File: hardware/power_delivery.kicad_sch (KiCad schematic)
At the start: 15 parts, among them J2 24V, U2 LM2596S-ADJ, U3 LM1117-5.0, U4 LM1117-3.3

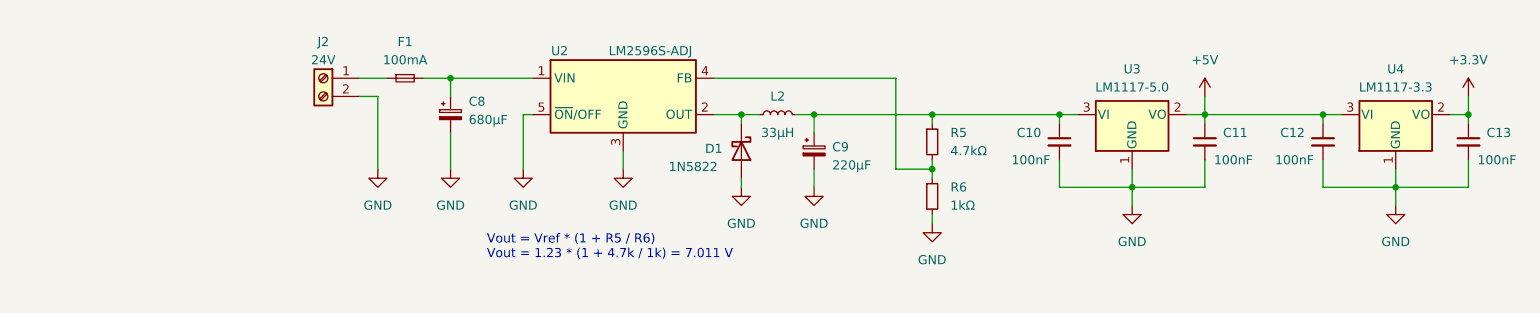
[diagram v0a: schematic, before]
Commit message: Improve the CAN transceiver circuit
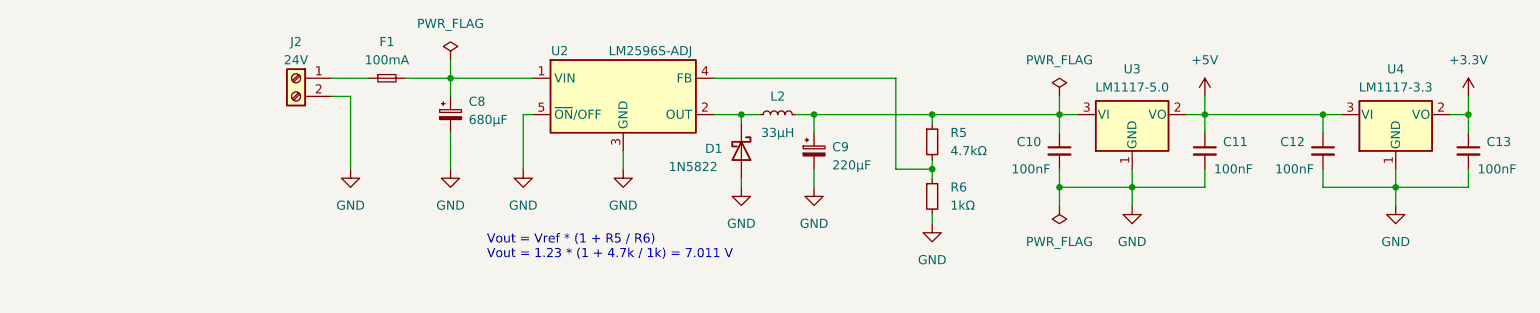
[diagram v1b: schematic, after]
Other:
- company: PUT MotorSport -> PUT Motorsport
- moved on the sheet: C10, C11, C12, C13, F1, J2

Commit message: Add a low-pass filter to the analog circuit supply
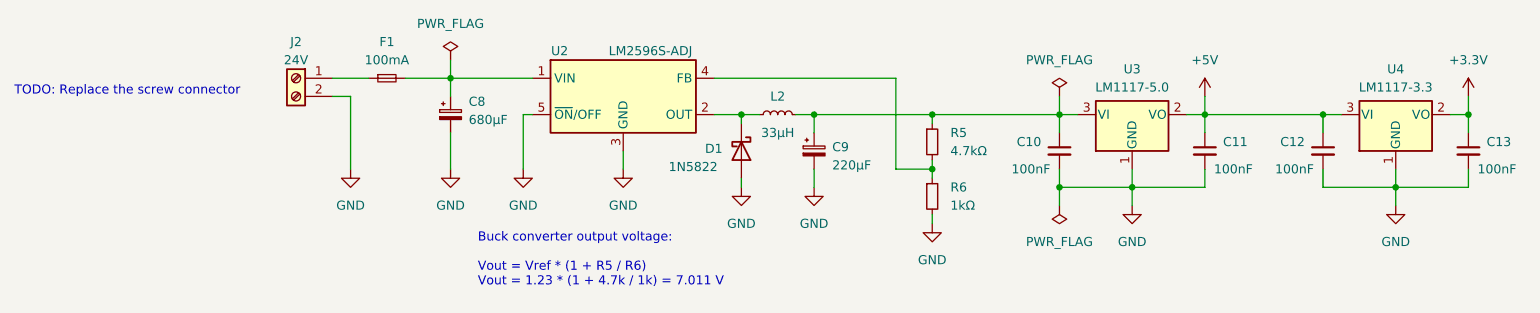
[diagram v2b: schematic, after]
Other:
- note added: "Buck converter output voltage: Vout = Vref * (1 + R5 / R6) Vout = 1.23 * (1 + 4.7k / 1k) = 7.011 V"
- note added: "TODO: Replace the screw connector"
- note removed: "Vout = Vref * (1 + R5 / R6) Vout = 1.23 * (1 + 4.7k / 1k) = 7.011 V"
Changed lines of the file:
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@@
     (stroke (width 0) (type default) (color 0 0 0 0))
   )
-  (text "Vout = Vref * (1 + R5 / R6)\nVout = 1.23 * (1 + 4.7k / 1k) = 7.011 V"
-    (at 90.17 113.03 0)
+  (text "Buck converter output voltage:\n\nVout = Vref * (1 + R5 / R6)\nVout = 1.23 * (1 + 4.7k / 1k) = 7.011 V"
+    (at 88.9 116.84 0)
     (effects (font (size 1.27 1.27)) (justify left bottom))
   )
+  (text "TODO: Replace the screw connector" (at 24.13 90.17 0)
+    (effects (font (size 1.27 1.27)) (justify left bottom))
+  )

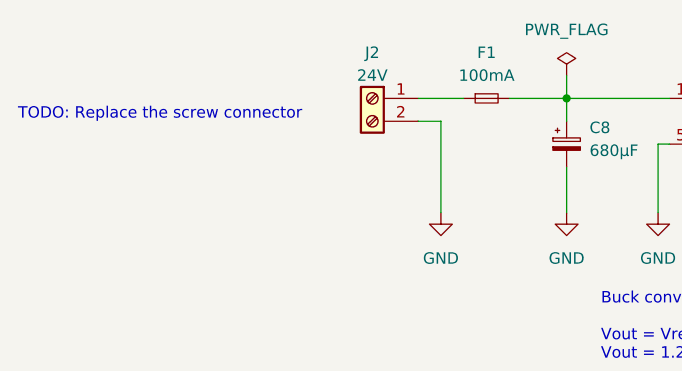
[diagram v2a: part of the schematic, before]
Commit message: Improve power delivery sheet:
- Move power connector to the main sheet
- Use PTC fuse
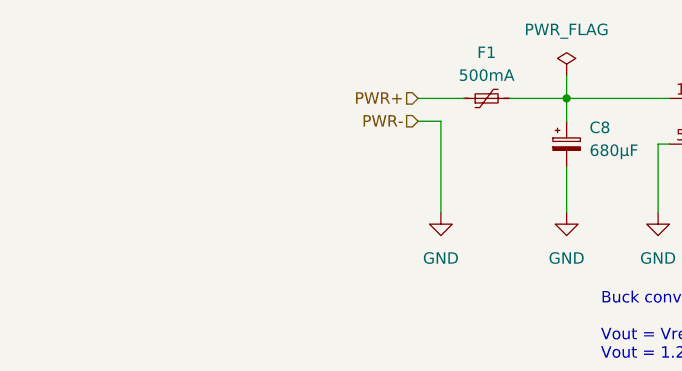
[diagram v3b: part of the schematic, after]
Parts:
- removed F1: 100mA, symbol Device:Fuse_Small
- removed J2: 24V, symbol Connector:Screw_Terminal_01x02
- added F1: 500mA, symbol Device:Polyfuse_Small
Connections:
- net at C8.1, U2.1 (VIN): now also F1.2
- new net PWR+: F1.1
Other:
- note removed: "TODO: Replace the screw connector"
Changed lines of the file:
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@@
     (effects (font (size 1.27 1.27)) (justify left bottom))
   )
-  (text "TODO: Replace the screw connector" (at 24.13 90.17 0)
-    (effects (font (size 1.27 1.27)) (justify left bottom))
+  (hierarchical_label "PWR+" (shape input) (at 68.58 87.63 180)
+    (effects (font (size 1.27 1.27)) (justify right))
+  )
+  (hierarchical_label "PWR-" (shape input) (at 68.58 90.17 180)
+    (effects (font (size 1.27 1.27)) (justify right))
   )
   (symbol (lib_id "power:GND") (at 180.34 105.41 0) (unit 1)
@@
     (pin "1")
   )
-  (symbol (lib_id "Connector:Screw_Terminal_01x02") (at 63.5 87.63 0) (mirror y) (unit 1)
-    (in_bom yes) (on_board yes)
-    (property "Reference" "J2" (id 0) (at 63.5 82.55 0))
-    (property "Value" "24V" (id 1) (at 63.5 85.09 0))
-    (property "Footprint" "" (id 2) (at 63.5 87.63 0)
-      (effects (font (size 1.27 1.27)) hide)
-    )
-    (property "Datasheet" "~" (id 3) (at 63.5 87.63 0)
-      (effects (font (size 1.27 1.27)) hide)
-    )
-    (pin "1")
-    (pin "2")
-  )
   (symbol (lib_id "power:GND") (at 109.22 100.33 0) (unit 1)
     (in_bom yes) (on_board yes) (fields_autoplaced)
@@
     )
     (pin "1")
+  )
+  (symbol (lib_id "Device:Polyfuse_Small") (at 76.2 87.63 90) (unit 1)
+    (in_bom yes) (on_board yes)
+    (property "Reference" "F1" (id 0) (at 76.2 82.55 90))
+    (property "Value" "500mA" (id 1) (at 76.2 85.09 90))
+    (property "Footprint" "" (id 2) (at 81.28 86.36 0)
+      (effects (font (size 1.27 1.27)) (justify left) hide)
+    )
+    (property "Datasheet" "~" (id 3) (at 76.2 87.63 0)
+      (effects (font (size 1.27 1.27)) hide)
+    )
+    (pin "1")
+    (pin "2")
   )
   (symbol (lib_id "Device:C_Small") (at 207.01 97.79 0) (unit 1)
@@
       (effects (font (size 1.27 1.27)) hide)
     )
-    (pin "1")
-    (pin "2")
-  )
-  (symbol (lib_id "Device:Fuse_Small") (at 76.2 87.63 0) (unit 1)
-    (in_bom yes) (on_board yes) (fields_autoplaced)
-    (property "Reference" "F1" (id 0) (at 76.2 82.55 0))
-    (property "Value" "100mA" (id 1) (at 76.2 85.09 0))
-    (property "Footprint" "" (id 2) (at 76.2 87.63 0)
-      (effects (font (size 1.27 1.27)) hide)
-    )
-    (property "Datasheet" "~" (id 3) (at 76.2 87.63 0)
-      (effects (font (size 1.27 1.27)) hide)
-    )

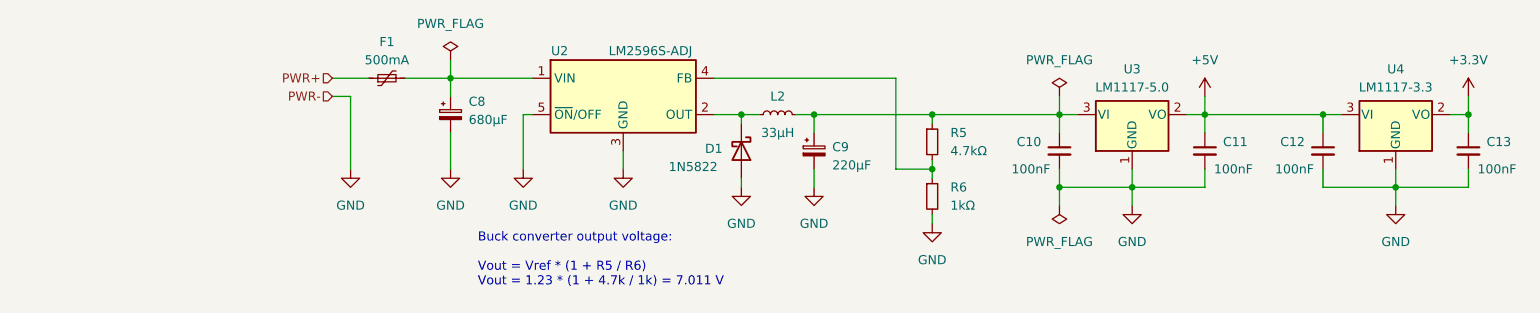
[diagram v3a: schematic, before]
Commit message: Refactor the main sheet
- Replace screw connectors with a goldpin header
- Add reset button
- Add SWD debugger header
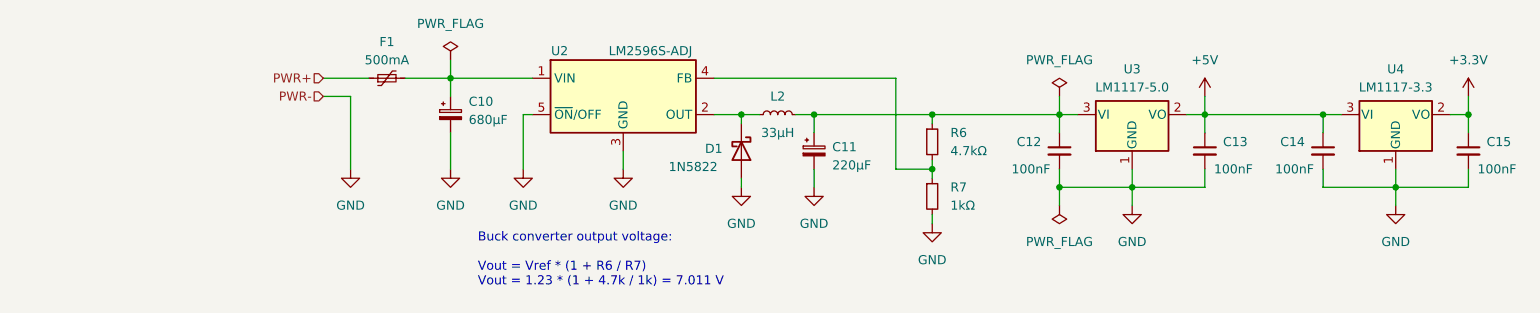
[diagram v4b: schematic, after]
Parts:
- renumbered C8 to C10, C9 to C11, C10 to C12, C11 to C13, C12 to C14, C13 to C15, R5 to R6, R6 to R7
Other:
- note added: "Buck converter output voltage: Vout = Vref * (1 + R6 / R7) Vout = 1.23 * (1 + 4.7k / 1k) = 7.011 V"
- note removed: "Buck converter output voltage: Vout = Vref * (1 + R5 / R6) Vout = 1.23 * (1 + 4.7k / 1k) = 7.011 V"
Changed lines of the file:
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@@
     (stroke (width 0) (type default) (color 0 0 0 0))
   )
-  (wire (pts (xy 68.58 87.63) (xy 73.66 87.63))
+  (wire (pts (xy 67.31 87.63) (xy 73.66 87.63))
     (stroke (width 0) (type default) (color 0 0 0 0))
   )
@@
     (stroke (width 0) (type default) (color 0 0 0 0))
   )
-  (wire (pts (xy 68.58 90.17) (xy 71.12 90.17))
+  (wire (pts (xy 67.31 90.17) (xy 71.12 90.17))
     (stroke (width 0) (type default) (color 0 0 0 0))
   )
@@
     (stroke (width 0) (type default) (color 0 0 0 0))
   )
-  (text "Buck converter output voltage:\n\nVout = Vref * (1 + R5 / R6)\nVout = 1.23 * (1 + 4.7k / 1k) = 7.011 V"
+  (text "Buck converter output voltage:\n\nVout = Vref * (1 + R6 / R7)\nVout = 1.23 * (1 + 4.7k / 1k) = 7.011 V"
     (at 88.9 116.84 0)
     (effects (font (size 1.27 1.27)) (justify left bottom))
   )
-  (hierarchical_label "PWR+" (shape input) (at 68.58 87.63 180)
+  (hierarchical_label "PWR+" (shape input) (at 67.31 87.63 180)
     (effects (font (size 1.27 1.27)) (justify right))
   )
-  (hierarchical_label "PWR-" (shape input) (at 68.58 90.17 180)
+  (hierarchical_label "PWR-" (shape input) (at 67.31 90.17 180)
     (effects (font (size 1.27 1.27)) (justify right))
   )
@@
   (symbol (lib_id "Device:C_Small") (at 227.33 97.79 0) (unit 1)
     (in_bom yes) (on_board yes)
-    (property "Reference" "C13" (id 0) (at 229.87 96.5262 0)
+    (property "Reference" "C15" (id 0) (at 229.87 96.5262 0)
       (effects (font (size 1.27 1.27)) (justify left))
     )
@@
   (symbol (lib_id "Device:C_Small") (at 207.01 97.79 0) (unit 1)
     (in_bom yes) (on_board yes)
-    (property "Reference" "C12" (id 0) (at 204.47 96.5262 0)
+    (property "Reference" "C14" (id 0) (at 204.47 96.5262 0)
       (effects (font (size 1.27 1.27)) (justify right))
     )
@@
   (symbol (lib_id "Device:C_Small") (at 190.5 97.79 0) (unit 1)
     (in_bom yes) (on_board yes)
-    (property "Reference" "C11" (id 0) (at 193.04 96.5262 0)
+    (property "Reference" "C13" (id 0) (at 193.04 96.5262 0)
       (effects (font (size 1.27 1.27)) (justify left))
     )
@@
   (symbol (lib_id "Device:R_Small") (at 152.4 104.14 0) (unit 1)
     (in_bom yes) (on_board yes)
-    (property "Reference" "R6" (id 0) (at 154.94 102.8699 0)
+    (property "Reference" "R7" (id 0) (at 154.94 102.8699 0)
       (effects (font (size 1.27 1.27)) (justify left))
     )
@@
   (symbol (lib_id "Device:C_Polarized_Small") (at 135.89 97.79 0) (unit 1)
     (in_bom yes) (on_board yes)
-    (property "Reference" "C9" (id 0) (at 138.43 97.2438 0)
+    (property "Reference" "C11" (id 0) (at 138.43 97.2438 0)
       (effects (font (size 1.27 1.27)) (justify left))
     )
@@
   (symbol (lib_id "Device:C_Polarized_Small") (at 85.09 92.71 0) (unit 1)
     (in_bom yes) (on_board yes) (fields_autoplaced)
-    (property "Reference" "C8" (id 0) (at 87.63 90.8938 0)
+    (property "Reference" "C10" (id 0) (at 87.63 90.8938 0)
       (effects (font (size 1.27 1.27)) (justify left))
     )
@@
   (symbol (lib_id "Device:C_Small") (at 170.18 97.79 0) (unit 1)
     (in_bom yes) (on_board yes)
-    (property "Reference" "C10" (id 0) (at 167.64 96.5262 0)
+    (property "Reference" "C12" (id 0) (at 167.64 96.5262 0)
       (effects (font (size 1.27 1.27)) (justify right))
     )
@@
   (symbol (lib_id "Device:R_Small") (at 152.4 96.52 0) (unit 1)
     (in_bom yes) (on_board yes)
-    (property "Reference" "R5" (id 0) (at 154.94 95.2499 0)
-      (effects (font (size 1.27 1.27)) (justify left))
-    )
+    (property "Reference" "R6" (id 0) (at 154.94 95.2499 0)
+      (effects (font (size 1.27 1.27)) (justify left))
+    )

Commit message: Add ADC circuit
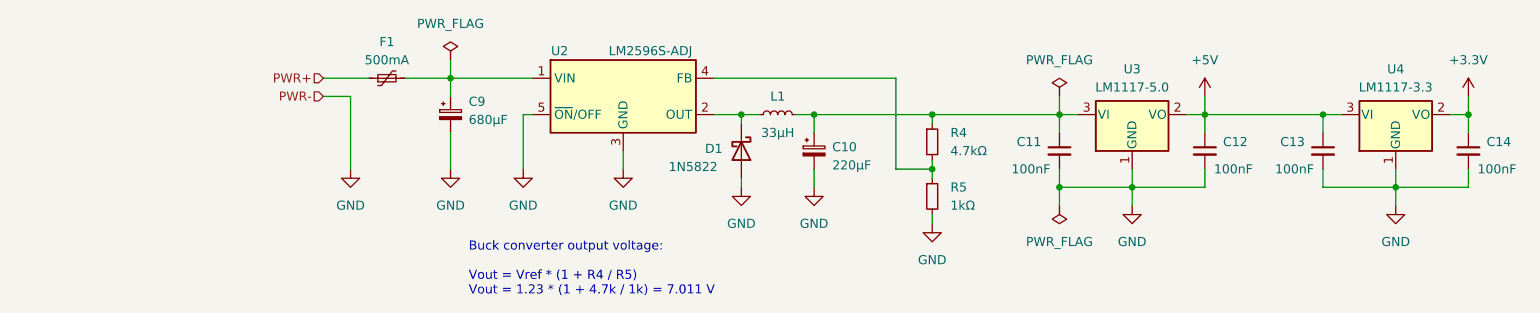
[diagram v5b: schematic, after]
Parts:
- renumbered C11 to C10, C12 to C11, C13 to C12, C14 to C13, C15 to C14, C10 to C9, L2 to L1, R6 to R4, R7 to R5
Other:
- note added: "Buck converter output voltage: Vout = Vref * (1 + R4 / R5) Vout = 1.23 * (1 + 4.7k / 1k) = 7.011 V"
- note removed: "Buck converter output voltage: Vout = Vref * (1 + R6 / R7) Vout = 1.23 * (1 + 4.7k / 1k) = 7.011 V"
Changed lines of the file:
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@@
   (title_block
     (title "Power Delivery")
-    (date "2022-11-21")
+    (date "2022-12-04")
     (rev "0.1.0")
     (company "PUT Motorsport")
+    (comment 1 "Author: I. Kajdan")
   )
   (junction (at 170.18 102.87) (diameter 0) (color 0 0 0 0)
@@
     (stroke (width 0) (type default) (color 0 0 0 0))
   )
-  (text "Buck converter output voltage:\n\nVout = Vref * (1 + R6 / R7)\nVout = 1.23 * (1 + 4.7k / 1k) = 7.011 V"
-    (at 88.9 116.84 0)
+  (text "Buck converter output voltage:\n\nVout = Vref * (1 + R4 / R5)\nVout = 1.23 * (1 + 4.7k / 1k) = 7.011 V"
+    (at 87.63 118.11 0)
     (effects (font (size 1.27 1.27)) (justify left bottom))
   )
@@
   (symbol (lib_id "Device:C_Small") (at 227.33 97.79 0) (unit 1)
     (in_bom yes) (on_board yes)
-    (property "Reference" "C15" (id 0) (at 229.87 96.5262 0)
+    (property "Reference" "C14" (id 0) (at 229.87 96.5262 0)
       (effects (font (size 1.27 1.27)) (justify left))
     )
@@
   (symbol (lib_id "Device:C_Small") (at 207.01 97.79 0) (unit 1)
     (in_bom yes) (on_board yes)
-    (property "Reference" "C14" (id 0) (at 204.47 96.5262 0)
+    (property "Reference" "C13" (id 0) (at 204.47 96.5262 0)
       (effects (font (size 1.27 1.27)) (justify right))
     )
@@
   (symbol (lib_id "Device:L_Small") (at 130.81 92.71 90) (unit 1)
     (in_bom yes) (on_board yes)
-    (property "Reference" "L2" (id 0) (at 130.81 90.17 90))
+    (property "Reference" "L1" (id 0) (at 130.81 90.17 90))
     (property "Value" "33μH" (id 1) (at 130.81 95.25 90))
     (property "Footprint" "" (id 2) (at 130.81 92.71 0)
@@
   (symbol (lib_id "Device:C_Small") (at 190.5 97.79 0) (unit 1)
     (in_bom yes) (on_board yes)
-    (property "Reference" "C13" (id 0) (at 193.04 96.5262 0)
+    (property "Reference" "C12" (id 0) (at 193.04 96.5262 0)
       (effects (font (size 1.27 1.27)) (justify left))
     )
@@
   (symbol (lib_id "Device:R_Small") (at 152.4 104.14 0) (unit 1)
     (in_bom yes) (on_board yes)
-    (property "Reference" "R7" (id 0) (at 154.94 102.8699 0)
+    (property "Reference" "R5" (id 0) (at 154.94 102.8699 0)
       (effects (font (size 1.27 1.27)) (justify left))
     )
@@
   (symbol (lib_id "Device:C_Polarized_Small") (at 135.89 97.79 0) (unit 1)
     (in_bom yes) (on_board yes)
-    (property "Reference" "C11" (id 0) (at 138.43 97.2438 0)
+    (property "Reference" "C10" (id 0) (at 138.43 97.2438 0)
       (effects (font (size 1.27 1.27)) (justify left))
     )
@@
   (symbol (lib_id "Device:C_Polarized_Small") (at 85.09 92.71 0) (unit 1)
     (in_bom yes) (on_board yes) (fields_autoplaced)
-    (property "Reference" "C10" (id 0) (at 87.63 90.8938 0)
+    (property "Reference" "C9" (id 0) (at 87.63 90.8938 0)
       (effects (font (size 1.27 1.27)) (justify left))
     )
@@
   (symbol (lib_id "Device:C_Small") (at 170.18 97.79 0) (unit 1)
     (in_bom yes) (on_board yes)
-    (property "Reference" "C12" (id 0) (at 167.64 96.5262 0)
+    (property "Reference" "C11" (id 0) (at 167.64 96.5262 0)
       (effects (font (size 1.27 1.27)) (justify right))
     )
@@
   (symbol (lib_id "Device:R_Small") (at 152.4 96.52 0) (unit 1)
     (in_bom yes) (on_board yes)
-    (property "Reference" "R6" (id 0) (at 154.94 95.2499 0)
-      (effects (font (size 1.27 1.27)) (justify left))
-    )
+    (property "Reference" "R4" (id 0) (at 154.94 95.2499 0)
+      (effects (font (size 1.27 1.27)) (justify left))
+    )
